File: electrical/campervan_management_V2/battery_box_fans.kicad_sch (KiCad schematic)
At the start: 11 parts, among them J9 Fans, U17 LTV-817S-TA1-C, U18 LTV-817S-TA1-C, U20 LTV-817S-TA1-C, U21 LTV-817S-TA1-C

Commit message: updated
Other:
- moved on the sheet: R4, R5
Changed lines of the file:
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@@
 	(text "Battery Box Fan2 Control"
 		(exclude_from_sim no)
-		(at 55.88 110.49 0)
+		(at 76.2 110.49 0)
 		(effects
 			(font
@@
 	(text "Battery Box Fan1 Control"
 		(exclude_from_sim no)
-		(at 55.88 95.25 0)
+		(at 76.2 95.25 0)
 		(effects
 			(font
@@
 	(text "Battery Box Fan2 Sensor"
 		(exclude_from_sim no)
-		(at 55.88 81.28 0)
+		(at 76.2 81.28 0)
 		(effects
 			(font
@@
 	)
 	(junction
-		(at 83.82 77.47)
+		(at 85.09 77.47)
 		(diameter 0)
 		(color 0 0 0 0)
@@
 	)
 	(junction
-		(at 87.63 60.96)
+		(at 85.09 60.96)
 		(diameter 0)
 		(color 0 0 0 0)
@@
 	(wire
 		(pts
-			(xy 71.12 66.04) (xy 71.12 96.52)
-		)
-		(stroke
-			(width 0)
-			(type default)
-		)
-	)
-	(wire
-		(pts
-			(xy 87.63 60.96) (xy 93.98 60.96)
-		)
-		(stroke
-			(width 0)
-			(type default)
-		)
-	)
-	(wire
-		(pts
-			(xy 40.64 60.96) (xy 87.63 60.96)
-		)
-		(stroke
-			(width 0)
-			(type default)
-		)
-	)
-	(wire
-		(pts
-			(xy 83.82 76.2) (xy 83.82 77.47)
-		)
-		(stroke
-			(width 0)
-			(type default)
-		)
-	)
-	(wire
-		(pts
-			(xy 87.63 50.8) (xy 87.63 52.07)
-		)
-		(stroke
-			(width 0)
-			(type default)
-		)
-	)
-	(wire
-		(pts
-			(xy 40.64 68.58) (xy 67.31 68.58)
-		)
-		(stroke
-			(width 0)
-			(type default)
-		)
-	)
-	(wire
-		(pts
-			(xy 74.93 63.5) (xy 74.93 77.47)
+			(xy 67.31 66.04) (xy 67.31 96.52)
+		)
+		(stroke
+			(width 0)
+			(type default)
+		)
+	)
+	(wire
+		(pts
+			(xy 85.09 60.96) (xy 93.98 60.96)
+		)
+		(stroke
+			(width 0)
+			(type default)
+		)
+	)
+	(wire
+		(pts
+			(xy 40.64 60.96) (xy 85.09 60.96)
+		)
+		(stroke
+			(width 0)
+			(type default)
+		)
+	)
+	(wire
+		(pts
+			(xy 85.09 76.2) (xy 85.09 77.47)
+		)
+		(stroke
+			(width 0)
+			(type default)
+		)
+	)
+	(wire
+		(pts
+			(xy 85.09 50.8) (xy 85.09 52.07)
+		)
+		(stroke
+			(width 0)
+			(type default)
+		)
+	)
+	(wire
+		(pts
+			(xy 40.64 68.58) (xy 63.5 68.58)
+		)
+		(stroke
+			(width 0)
+			(type default)
+		)
+	)
+	(wire
+		(pts
+			(xy 71.12 63.5) (xy 71.12 77.47)
 		)
 		(stroke
@@
 	(wire
 		(pts
-			(xy 67.31 68.58) (xy 67.31 111.76)
-		)
-		(stroke
-			(width 0)
-			(type default)
-		)
-	)
-	(wire
-		(pts
-			(xy 74.93 77.47) (xy 83.82 77.47)
+			(xy 63.5 68.58) (xy 63.5 111.76)
+		)
+		(stroke
+			(width 0)
+			(type default)
+		)
+	)
+	(wire
+		(pts
+			(xy 71.12 77.47) (xy 85.09 77.47)
 		)
 		(stroke
@@
 	(wire
 		(pts
-			(xy 87.63 59.69) (xy 87.63 60.96)
-		)
-		(stroke
-			(width 0)
-			(type default)
-		)
-	)
-	(wire
-		(pts
-			(xy 40.64 63.5) (xy 74.93 63.5)
-		)
-		(stroke
-			(width 0)
-			(type default)
-		)
-	)
-	(wire
-		(pts
-			(xy 83.82 66.04) (xy 83.82 68.58)
+			(xy 85.09 59.69) (xy 85.09 60.96)
+		)
+		(stroke
+			(width 0)
+			(type default)
+		)
+	)
+	(wire
+		(pts
+			(xy 40.64 63.5) (xy 71.12 63.5)
+		)
+		(stroke
+			(width 0)
+			(type default)
+		)
+	)
+	(wire
+		(pts
+			(xy 85.09 66.04) (xy 85.09 68.58)
 		)
 		(stroke
@@
 	(wire
 		(pts
-			(xy 83.82 77.47) (xy 93.98 77.47)
+			(xy 85.09 77.47) (xy 93.98 77.47)
 		)
 		(stroke
@@
 	(wire
 		(pts
-			(xy 67.31 111.76) (xy 93.98 111.76)
-		)
-		(stroke
-			(width 0)
-			(type default)
-		)
-	)
-	(wire
-		(pts
-			(xy 71.12 96.52) (xy 93.98 96.52)
+			(xy 63.5 111.76) (xy 93.98 111.76)
+		)
+		(stroke
+			(width 0)
+			(type default)
+		)
+	)
+	(wire
+		(pts
+			(xy 67.31 96.52) (xy 93.98 96.52)
 		)
 		(stroke
@@
 	(wire
 		(pts
-			(xy 40.64 66.04) (xy 71.12 66.04)
+			(xy 40.64 66.04) (xy 67.31 66.04)
 		)
 		(stroke
@@
 	(wire
 		(pts
-			(xy 81.28 66.04) (xy 83.82 66.04)
-		)
-		(stroke
-			(width 0)
-			(type default)
-		)
-	)
-	(wire
-		(pts
-			(xy 83.82 50.8) (xy 87.63 50.8)
+			(xy 82.55 66.04) (xy 85.09 66.04)
+		)
+		(stroke
+			(width 0)
+			(type default)
+		)
+	)
+	(wire
+		(pts
+			(xy 81.28 50.8) (xy 85.09 50.8)
 		)
 		(stroke
@@
 	(global_label "VIN"
 		(shape input)
-		(at 83.82 50.8 180)
+		(at 81.28 50.8 180)
 		(fields_autoplaced yes)
 		(effects
@@
 		)
 		(property "Intersheetrefs" "${INTERSHEET_REFS}"
-			(at 77.8109 50.8 0)
+			(at 75.2709 50.8 0)
 			(effects
 				(font
@@
 	(global_label "VIN"
 		(shape input)
-		(at 81.28 66.04 180)
+		(at 82.55 66.04 180)
 		(fields_autoplaced yes)
 		(effects
@@
 		)
 		(property "Intersheetrefs" "${INTERSHEET_REFS}"
-			(at 75.2709 66.04 0)
+			(at 76.5409 66.04 0)
 			(effects
 				(font
@@
 	(symbol
 		(lib_id "Device:R")
-		(at 87.63 55.88 0)
+		(at 85.09 55.88 0)
 		(unit 1)
 		(exclude_from_sim no)
@@
 		(fields_autoplaced yes)
 		(property "Reference" "R4"
-			(at 90.17 54.6099 0)
+			(at 87.63 54.6099 0)
 			(effects
 				(font
@@
 		)
 		(property "Value" "47k"
-			(at 90.17 57.1499 0)
+			(at 87.63 57.1499 0)
 			(effects
 				(font
@@
 		)
 		(property "Footprint" "Resistor_SMD:R_0805_2012Metric"
-			(at 85.852 55.88 90)
+			(at 83.312 55.88 90)
 			(effects
 				(font
@@
 		)
 		(property "Datasheet" "~"
-			(at 87.63 55.88 0)
+			(at 85.09 55.88 0)
 			(effects
 				(font
@@
 		)
 		(property "Description" "Resistor"
-			(at 87.63 55.88 0)
+			(at 85.09 55.88 0)
 			(effects
 				(font
@@
 		)
 		(property "LCSC PN" "C17713"
-			(at 87.63 55.88 0)
+			(at 85.09 55.88 0)
 			(effects
 				(font
@@
 		)
 		(property "Extended" "B"
-			(at 87.63 55.88 0)
+			(at 85.09 55.88 0)
 			(effects
 				(font
@@
 	(symbol
 		(lib_id "Device:R")
-		(at 83.82 72.39 0)
+		(at 85.09 72.39 0)
 		(unit 1)
 		(exclude_from_sim no)
@@
 		(fields_autoplaced yes)
 		(property "Reference" "R5"
-			(at 86.36 71.1199 0)
+			(at 87.63 71.1199 0)
 			(effects
 				(font
@@
 		)
 		(property "Value" "47k"
-			(at 86.36 73.6599 0)
+			(at 87.63 73.6599 0)
 			(effects
 				(font
@@
 		)
 		(property "Footprint" "Resistor_SMD:R_0805_2012Metric"
-			(at 82.042 72.39 90)
+			(at 83.312 72.39 90)
 			(effects
 				(font
@@
 		)
 		(property "Datasheet" "~"
-			(at 83.82 72.39 0)
+			(at 85.09 72.39 0)
 			(effects
 				(font
@@
 		)
 		(property "Description" "Resistor"
-			(at 83.82 72.39 0)
+			(at 85.09 72.39 0)
 			(effects
 				(font
@@
 		)
 		(property "LCSC PN" "C17713"
-			(at 83.82 72.39 0)
+			(at 85.09 72.39 0)
 			(effects
 				(font
@@
 		)
 		(property "Extended" "B"
-			(at 83.82 72.39 0)
-			(effects
-				(font
+			(at 85.09 72.39 0)
+			(effects
+				(font

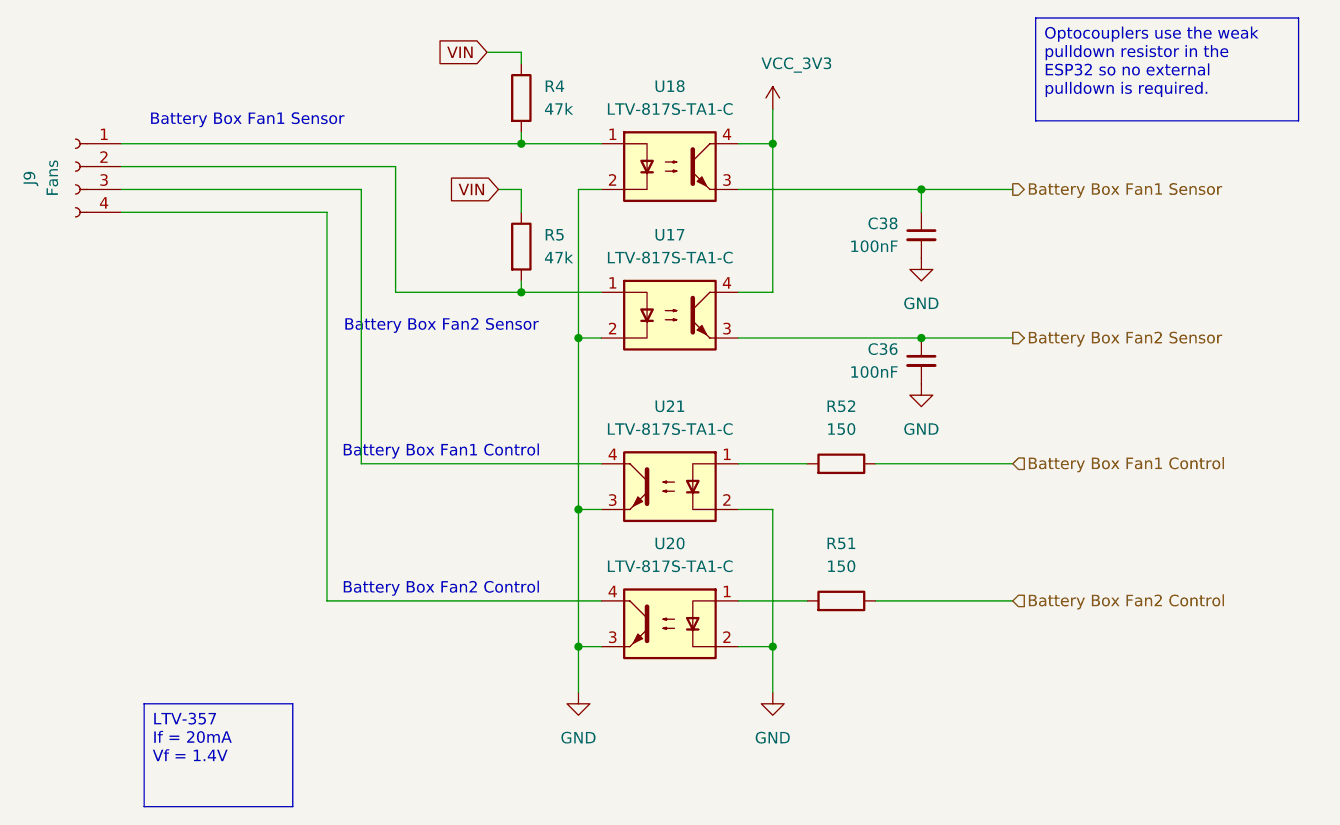
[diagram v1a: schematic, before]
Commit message: First attempt at PCB layout
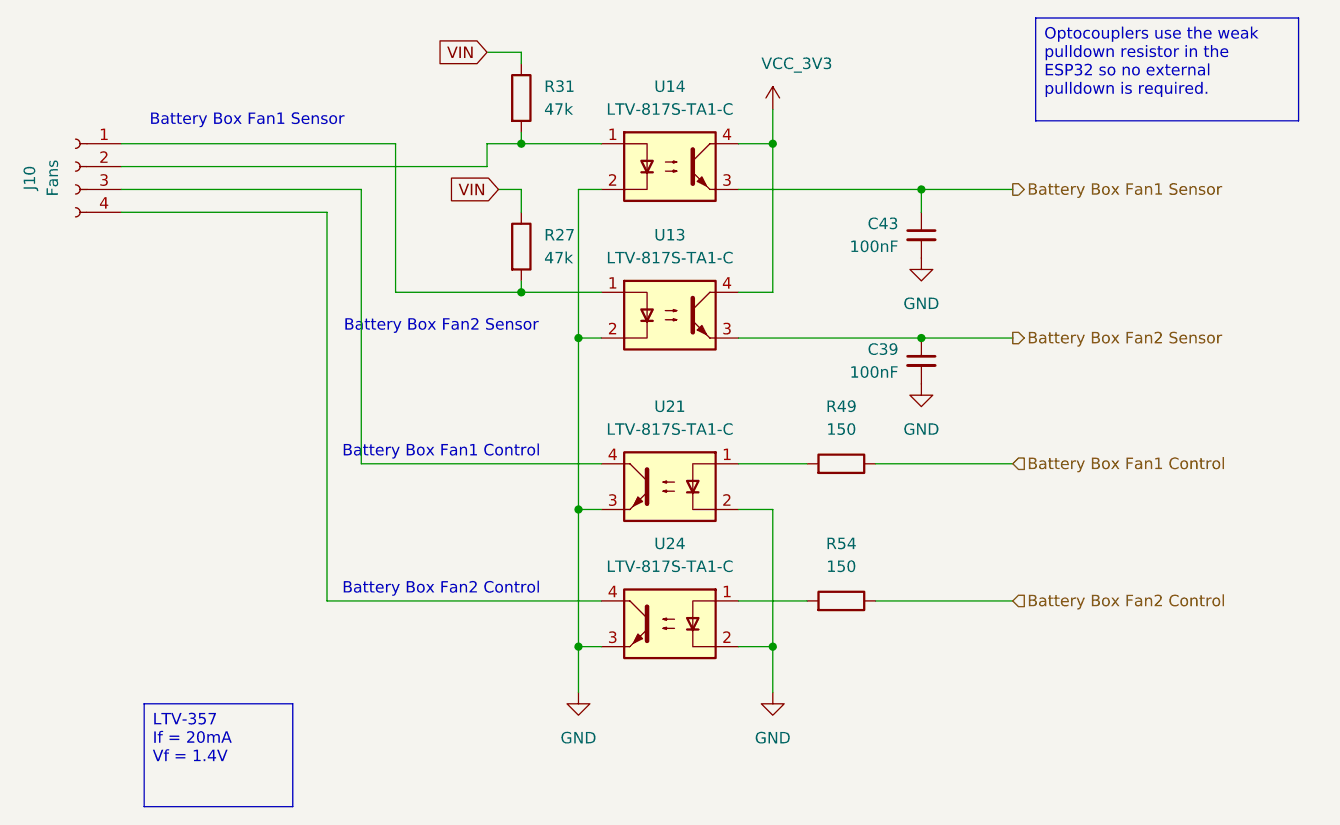
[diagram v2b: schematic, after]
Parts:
- renumbered C36 to C39, C38 to C43, J9 to J10, R5 to R27, R4 to R31, R52 to R49, R51 to R54, U17 to U13, U18 to U14, U20 to U24
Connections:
- net at R31.2, U14.1: now also J10.2 (Pin_2); no longer J10.1 (Pin_1)
- net at R27.2, U13.1: now also J10.1 (Pin_1); no longer J10.2 (Pin_2)
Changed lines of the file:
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@@
 	(wire
 		(pts
-			(xy 40.64 60.96) (xy 85.09 60.96)
+			(xy 40.64 60.96) (xy 71.12 60.96)
 		)
 		(stroke
@@
 	(wire
 		(pts
-			(xy 71.12 63.5) (xy 71.12 77.47)
+			(xy 71.12 60.96) (xy 71.12 77.47)
+		)
+		(stroke
+			(width 0)
+			(type default)
+		)
+	)
+	(wire
+		(pts
+			(xy 81.28 63.5) (xy 81.28 60.96)
 		)
 		(stroke
@@
 	(wire
 		(pts
+			(xy 81.28 60.96) (xy 85.09 60.96)
+		)
+		(stroke
+			(width 0)
+			(type default)
+		)
+	)
+	(wire
+		(pts
 			(xy 129.54 66.04) (xy 139.7 66.04)
 		)
@@
 	(wire
 		(pts
-			(xy 40.64 63.5) (xy 71.12 63.5)
-		)
-		(stroke
-			(width 0)
-			(type default)
-		)
-	)
-	(wire
-		(pts
 			(xy 85.09 66.04) (xy 85.09 68.58)
 		)
@@
 		(pts
 			(xy 91.44 101.6) (xy 91.44 116.84)
+		)
+		(stroke
+			(width 0)
+			(type default)
+		)
+	)
+	(wire
+		(pts
+			(xy 40.64 63.5) (xy 81.28 63.5)
 		)
 		(stroke
@@
 		(dnp no)
 		(fields_autoplaced yes)
-		(property "Reference" "R4"
+		(property "Reference" "R31"
 			(at 87.63 54.6099 0)
 			(effects
@@
 			(project "campervan_management_V2"
 				(path "/870a08cc-a6e6-4310-b4b3-ae6af01530aa/0e33b410-b50b-448f-85fa-90a1aeab9694"
-					(reference "R4")
+					(reference "R31")
 					(unit 1)
 				)
@@
 		(on_board yes)
 		(dnp no)
-		(property "Reference" "J9"
+		(property "Reference" "J10"
 			(at 30.48 64.77 90)
 			(effects
@@
 			(project "campervan_management_V2"
 				(path "/870a08cc-a6e6-4310-b4b3-ae6af01530aa/0e33b410-b50b-448f-85fa-90a1aeab9694"
-					(reference "J9")
+					(reference "J10")
 					(unit 1)
 				)
@@
 		(on_board yes)
 		(dnp no)
-		(property "Reference" "C36"
+		(property "Reference" "C39"
 			(at 127 83.8262 0)
 			(effects
@@
 			(project "campervan_management_V2"
 				(path "/870a08cc-a6e6-4310-b4b3-ae6af01530aa/0e33b410-b50b-448f-85fa-90a1aeab9694"
-					(reference "C36")
+					(reference "C39")
 					(unit 1)
 				)
@@
 		(dnp no)
 		(fields_autoplaced yes)
-		(property "Reference" "R51"
+		(property "Reference" "R54"
 			(at 120.65 105.41 90)
 			(effects
@@
 			(project "campervan_management_V2"
 				(path "/870a08cc-a6e6-4310-b4b3-ae6af01530aa/0e33b410-b50b-448f-85fa-90a1aeab9694"
-					(reference "R51")
+					(reference "R54")
 					(unit 1)
 				)
@@
 		(on_board yes)
 		(dnp no)
-		(property "Reference" "U20"
+		(property "Reference" "U24"
 			(at 101.6 105.41 0)
 			(effects
@@
 			(project "campervan_management_V2"
 				(path "/870a08cc-a6e6-4310-b4b3-ae6af01530aa/0e33b410-b50b-448f-85fa-90a1aeab9694"
-					(reference "U20")
+					(reference "U24")
 					(unit 1)
 				)
@@
 		(on_board yes)
 		(dnp no)
-		(property "Reference" "U18"
+		(property "Reference" "U14"
 			(at 101.6 54.61 0)
 			(effects
@@
 			(project ""
 				(path "/870a08cc-a6e6-4310-b4b3-ae6af01530aa/0e33b410-b50b-448f-85fa-90a1aeab9694"
-					(reference "U18")
+					(reference "U14")
 					(unit 1)
 				)
@@
 		(on_board yes)
 		(dnp no)
-		(property "Reference" "C38"
+		(property "Reference" "C43"
 			(at 127 69.8562 0)
 			(effects
@@
 			(project "campervan_management_V2"
 				(path "/870a08cc-a6e6-4310-b4b3-ae6af01530aa/0e33b410-b50b-448f-85fa-90a1aeab9694"
-					(reference "C38")
+					(reference "C43")
 					(unit 1)
 				)
@@
 		(on_board yes)
 		(dnp no)
-		(property "Reference" "U17"
+		(property "Reference" "U13"
 			(at 101.6 71.12 0)
 			(effects
@@
 			(project "campervan_management_V2"
 				(path "/870a08cc-a6e6-4310-b4b3-ae6af01530aa/0e33b410-b50b-448f-85fa-90a1aeab9694"
-					(reference "U17")
+					(reference "U13")
 					(unit 1)
 				)
@@
 		(dnp no)
 		(fields_autoplaced yes)
-		(property "Reference" "R5"
+		(property "Reference" "R27"
 			(at 87.63 71.1199 0)
 			(effects
@@
 			(project "campervan_management_V2"
 				(path "/870a08cc-a6e6-4310-b4b3-ae6af01530aa/0e33b410-b50b-448f-85fa-90a1aeab9694"
-					(reference "R5")
+					(reference "R27")
 					(unit 1)
 				)
@@
 		(dnp no)
 		(fields_autoplaced yes)
-		(property "Reference" "R52"
+		(property "Reference" "R49"
 			(at 120.65 90.17 90)
 			(effects
@@
 			(project "campervan_management_V2"
 				(path "/870a08cc-a6e6-4310-b4b3-ae6af01530aa/0e33b410-b50b-448f-85fa-90a1aeab9694"
-					(reference "R52")
+					(reference "R49")
 					(unit 1)
 				)

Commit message: Close to final design
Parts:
- renumbered C43 to C23, C39 to C25, J10 to J6, R54 to R20, R49 to R23, R31 to R27, R27 to R28, U24 to U11, U21 to U13, U13 to U16
